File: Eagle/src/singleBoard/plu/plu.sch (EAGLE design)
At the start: 10 parts, among them J1 5787834-2

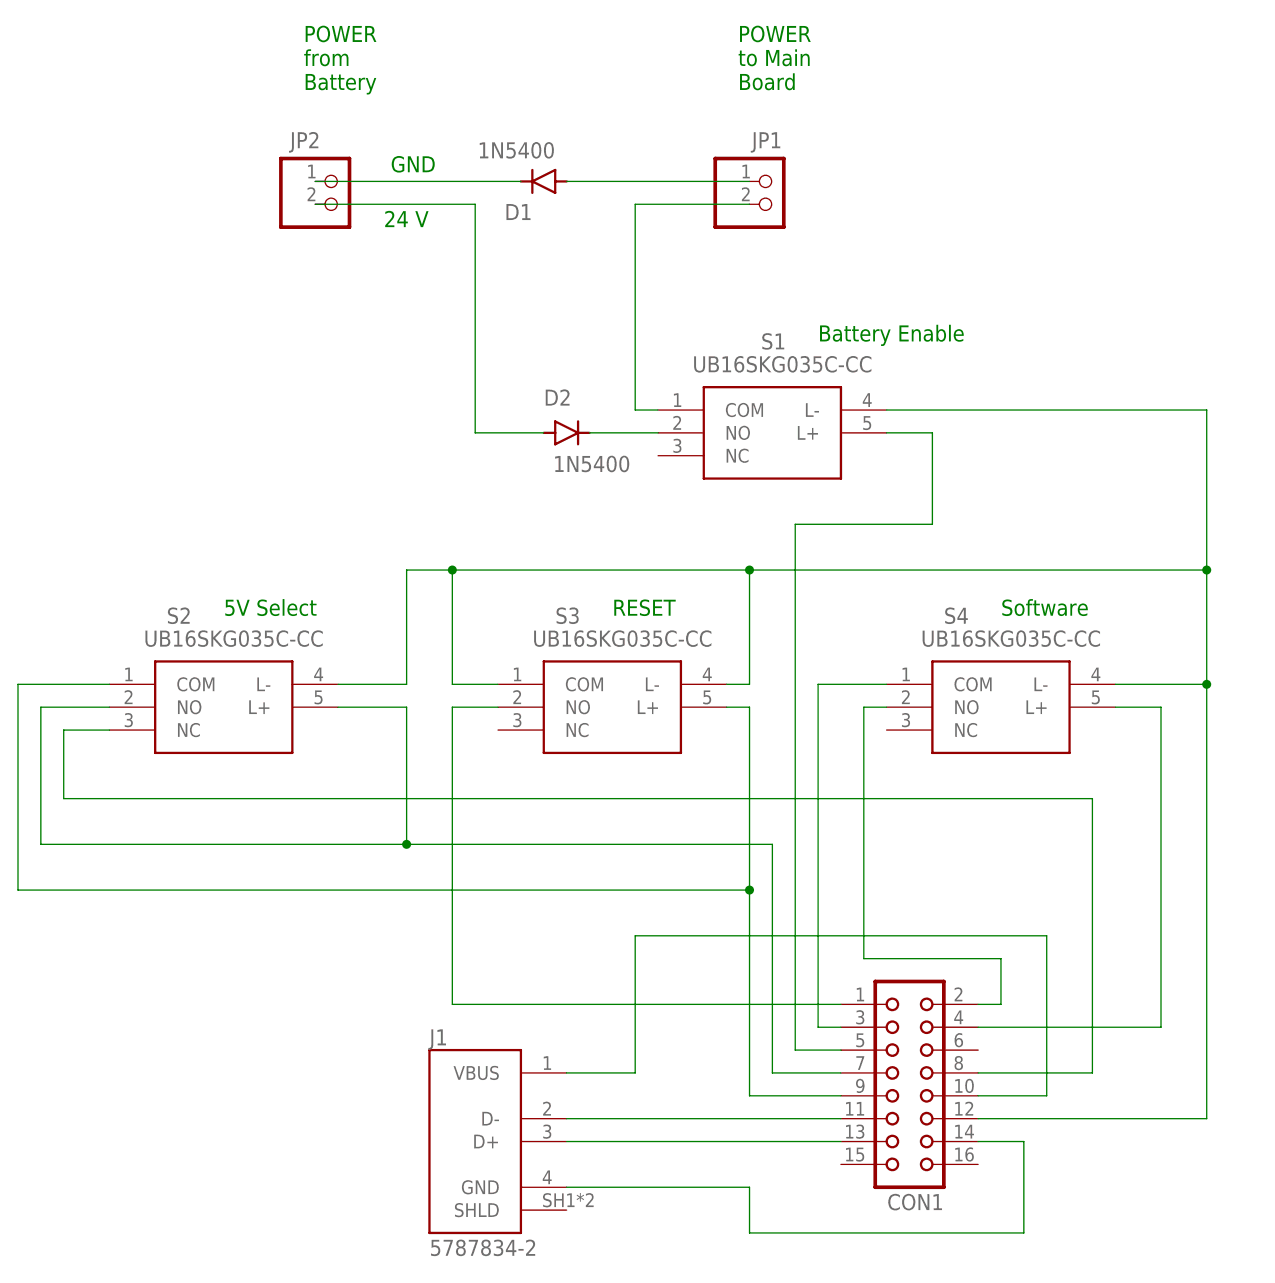
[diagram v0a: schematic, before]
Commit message: fix plu spacing issues found in flatcam
version P2 of PLU has a bunch of fixes to fix places where there were passages between traces, or between traces and pads that were too narrow for a 1/32 inch mill bit to pass through. 2 weren't fixable, and I added jumpers to dodge the issue. The rest of the 7 issues were resolved by small adjustments to trace locations
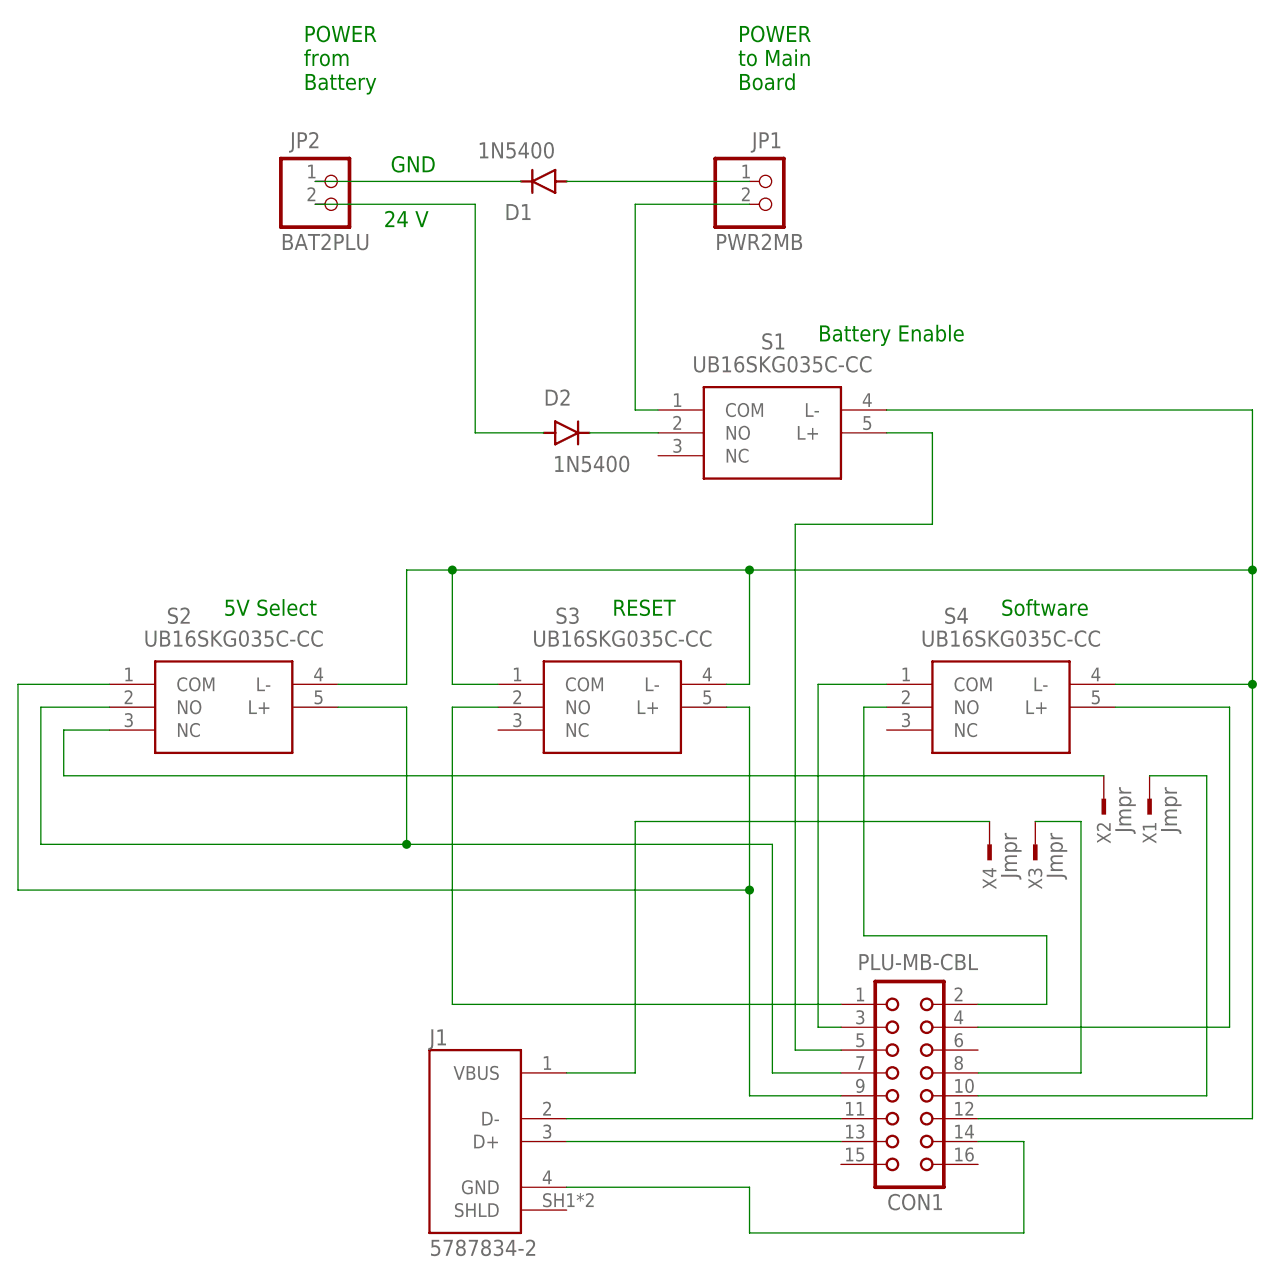
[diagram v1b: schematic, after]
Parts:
- added X1, X2, X3, X4: Jmpr, con-samtec:TSW-101-07-G-S
- CON1: value (none) -> PLU-MB-CBL
- JP1: value (none) -> PWR2MB
- JP2: value (none) -> BAT2PLU
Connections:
- new net N$25: S2.NC, X2.1
- new net N$28: CON1.8, X3.1
- net N$18: now also CON1.10, X1.1; no longer CON1.8, S2.NC
- net N$8: now also X4.1; no longer CON1.10
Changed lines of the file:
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@@
 </classes>
 <parts>
-<part name="CON1" library="con-harting" library_urn="urn:adsk.eagle:library:151" deviceset="CON16" device="" package3d_urn="urn:adsk.eagle:package:7118/1"/>
-<part name="JP2" library="pinhead" library_urn="urn:adsk.eagle:library:325" deviceset="PINHD-1X2" device="" package3d_urn="urn:adsk.eagle:package:22435/2"/>
+<part name="CON1" library="con-harting" library_urn="urn:adsk.eagle:library:151" deviceset="CON16" device="" package3d_urn="urn:adsk.eagle:package:7118/1" value="PLU-MB-CBL"/>
+<part name="JP2" library="pinhead" library_urn="urn:adsk.eagle:library:325" deviceset="PINHD-1X2" device="" package3d_urn="urn:adsk.eagle:package:22435/2" value="BAT2PLU"/>
 <part name="S1" library="UB16SKG035C-CC" deviceset="UB16SKG035C-CC" device=""/>
 <part name="S2" library="UB16SKG035C-CC" deviceset="UB16SKG035C-CC" device=""/>
 <part name="S3" library="UB16SKG035C-CC" deviceset="UB16SKG035C-CC" device=""/>
 <part name="S4" library="UB16SKG035C-CC" deviceset="UB16SKG035C-CC" device=""/>
-<part name="JP1" library="pinhead" library_urn="urn:adsk.eagle:library:325" deviceset="PINHD-1X2" device="" package3d_urn="urn:adsk.eagle:package:22435/2"/>
+<part name="JP1" library="pinhead" library_urn="urn:adsk.eagle:library:325" deviceset="PINHD-1X2" device="" package3d_urn="urn:adsk.eagle:package:22435/2" value="PWR2MB"/>
 <part name="J1" library="5787834-2" deviceset="5787834-2" device=""/>
 <part name="D1" library="diode" library_urn="urn:adsk.eagle:library:210" deviceset="1N5400" device="" package3d_urn="urn:adsk.eagle:package:43365/1"/>
 <part name="D2" library="diode" library_urn="urn:adsk.eagle:library:210" deviceset="1N5400" device="" package3d_urn="urn:adsk.eagle:package:43365/1"/>
+<part name="X1" library="con-samtec" library_urn="urn:adsk.eagle:library:184" deviceset="TSW-101-*-G-S" device="" technology="07" value="Jmpr"/>
+<part name="X2" library="con-samtec" library_urn="urn:adsk.eagle:library:184" deviceset="TSW-101-*-G-S" device="" technology="07" value="Jmpr"/>
+<part name="X3" library="con-samtec" library_urn="urn:adsk.eagle:library:184" deviceset="TSW-101-*-G-S" device="" technology="07" value="Jmpr"/>
+<part name="X4" library="con-samtec" library_urn="urn:adsk.eagle:library:184" deviceset="TSW-101-*-G-S" device="" technology="07" value="Jmpr"/>
 </parts>
 <sheets>
@@
 <instances>
 <instance part="CON1" gate="G$1" x="71.12" y="-116.84" smashed="yes" rot="R180">
-<attribute name="VALUE" x="74.93" y="-101.6" size="1.778" layer="96" rot="R180"/>
+<attribute name="VALUE" x="78.74" y="-101.092" size="1.778" layer="96" rot="R180"/>
 <attribute name="NAME" x="74.93" y="-127.762" size="1.778" layer="95" rot="R180"/>
 </instance>
@@
 <attribute name="NAME" x="30.48" y="-40.1574" size="1.778" layer="95"/>
 <attribute name="VALUE" x="31.496" y="-47.5234" size="1.778" layer="96"/>
+</instance>
+<instance part="X1" gate="-1" x="97.79" y="-83.82" smashed="yes" rot="R270">
+<attribute name="VALUE" x="99.06" y="-82.55" size="1.778" layer="96" rot="R270"/>
+<attribute name="NAME" x="97.028" y="-86.36" size="1.524" layer="95" rot="R270"/>
+</instance>
+<instance part="X2" gate="-1" x="92.71" y="-83.82" smashed="yes" rot="R270">
+<attribute name="VALUE" x="93.98" y="-82.55" size="1.778" layer="96" rot="R270"/>
+<attribute name="NAME" x="91.948" y="-86.36" size="1.524" layer="95" rot="R270"/>
+</instance>
+<instance part="X3" gate="-1" x="85.09" y="-88.9" smashed="yes" rot="R270">
+<attribute name="VALUE" x="86.36" y="-87.63" size="1.778" layer="96" rot="R270"/>
+<attribute name="NAME" x="84.328" y="-91.44" size="1.524" layer="95" rot="R270"/>
+</instance>
+<instance part="X4" gate="-1" x="80.01" y="-88.9" smashed="yes" rot="R270">
+<attribute name="VALUE" x="81.28" y="-87.63" size="1.778" layer="96" rot="R270"/>
+<attribute name="NAME" x="79.248" y="-91.44" size="1.524" layer="95" rot="R270"/>
 </instance>
 </instances>
@@
 <pinref part="JP1" gate="G$1" pin="2"/>
 <wire x1="40.64" y1="-17.78" x2="53.34" y2="-17.78" width="1.27" layer="91"/>
-</segment>
-</net>
-<net name="N$8" class="0">
-<segment>
-<wire x1="33.02" y1="-114.3" x2="40.64" y2="-114.3" width="0.1524" layer="91"/>
-<pinref part="J1" gate="G$1" pin="VBUS"/>
-<wire x1="40.64" y1="-114.3" x2="40.64" y2="-99.06" width="0.1524" layer="91"/>
-<wire x1="40.64" y1="-99.06" x2="86.36" y2="-99.06" width="0.1524" layer="91"/>
-<wire x1="86.36" y1="-99.06" x2="86.36" y2="-116.84" width="0.1524" layer="91"/>
-<pinref part="CON1" gate="G$1" pin="10"/>
-<wire x1="78.74" y1="-116.84" x2="86.36" y2="-116.84" width="0.1524" layer="91"/>
 </segment>
 </net>
@@
 <wire x1="66.04" y1="-73.66" x2="68.58" y2="-73.66" width="0.1524" layer="91"/>
 <pinref part="CON1" gate="G$1" pin="2"/>
-<wire x1="78.74" y1="-106.68" x2="81.28" y2="-106.68" width="0.1524" layer="91"/>
-<wire x1="81.28" y1="-106.68" x2="81.28" y2="-101.6" width="0.1524" layer="91"/>
-<wire x1="81.28" y1="-101.6" x2="66.04" y2="-101.6" width="0.1524" layer="91"/>
-<wire x1="66.04" y1="-101.6" x2="66.04" y2="-73.66" width="0.1524" layer="91"/>
+<wire x1="66.04" y1="-99.06" x2="66.04" y2="-73.66" width="0.1524" layer="91"/>
+<wire x1="66.04" y1="-99.06" x2="86.36" y2="-99.06" width="0.1524" layer="91"/>
+<wire x1="86.36" y1="-99.06" x2="86.36" y2="-106.68" width="0.1524" layer="91"/>
+<wire x1="86.36" y1="-106.68" x2="78.74" y2="-106.68" width="0.1524" layer="91"/>
 </segment>
 </net>
@@
 <segment>
 <pinref part="CON1" gate="G$1" pin="4"/>
-<wire x1="78.74" y1="-109.22" x2="99.06" y2="-109.22" width="0.1524" layer="91"/>
-<wire x1="99.06" y1="-109.22" x2="99.06" y2="-73.66" width="0.1524" layer="91"/>
+<wire x1="78.74" y1="-109.22" x2="106.68" y2="-109.22" width="0.1524" layer="91"/>
+<wire x1="106.68" y1="-109.22" x2="106.68" y2="-73.66" width="0.1524" layer="91"/>
 <pinref part="S4" gate="G$1" pin="L+"/>
-<wire x1="99.06" y1="-73.66" x2="93.98" y2="-73.66" width="0.1524" layer="91"/>
+<wire x1="106.68" y1="-73.66" x2="93.98" y2="-73.66" width="0.1524" layer="91"/>
 </segment>
 </net>
@@
 </segment>
 </net>
-<net name="N$18" class="0">
-<segment>
-<wire x1="91.44" y1="-114.3" x2="91.44" y2="-83.82" width="0.1524" layer="91"/>
-<wire x1="91.44" y1="-83.82" x2="-22.86" y2="-83.82" width="0.1524" layer="91"/>
-<wire x1="-22.86" y1="-83.82" x2="-22.86" y2="-76.2" width="0.1524" layer="91"/>
-<pinref part="S2" gate="G$1" pin="NC"/>
-<wire x1="-22.86" y1="-76.2" x2="-17.78" y2="-76.2" width="0.1524" layer="91"/>
-<pinref part="CON1" gate="G$1" pin="8"/>
-<wire x1="78.74" y1="-114.3" x2="91.44" y2="-114.3" width="0.1524" layer="91"/>
-</segment>
-</net>
 <net name="N$19" class="0">
 <segment>
@@
 <segment>
 <pinref part="CON1" gate="G$1" pin="12"/>
-<wire x1="78.74" y1="-119.38" x2="104.14" y2="-119.38" width="0.1524" layer="91"/>
-<wire x1="104.14" y1="-119.38" x2="104.14" y2="-71.12" width="0.1524" layer="91"/>
+<wire x1="78.74" y1="-119.38" x2="109.22" y2="-119.38" width="0.1524" layer="91"/>
+<wire x1="109.22" y1="-119.38" x2="109.22" y2="-71.12" width="0.1524" layer="91"/>
 <pinref part="S1" gate="G$1" pin="L-"/>
-<wire x1="104.14" y1="-71.12" x2="104.14" y2="-58.42" width="0.1524" layer="91"/>
-<wire x1="104.14" y1="-58.42" x2="104.14" y2="-40.64" width="0.1524" layer="91"/>
-<wire x1="104.14" y1="-40.64" x2="68.58" y2="-40.64" width="0.1524" layer="91"/>
-<wire x1="104.14" y1="-58.42" x2="53.34" y2="-58.42" width="0.1524" layer="91"/>
-<junction x="104.14" y="-58.42"/>
+<wire x1="109.22" y1="-71.12" x2="109.22" y2="-58.42" width="0.1524" layer="91"/>
+<wire x1="109.22" y1="-58.42" x2="109.22" y2="-40.64" width="0.1524" layer="91"/>
+<wire x1="109.22" y1="-40.64" x2="68.58" y2="-40.64" width="0.1524" layer="91"/>
+<wire x1="109.22" y1="-58.42" x2="53.34" y2="-58.42" width="0.1524" layer="91"/>
+<junction x="109.22" y="-58.42"/>
 <wire x1="53.34" y1="-58.42" x2="20.32" y2="-58.42" width="0.1524" layer="91"/>
 <wire x1="20.32" y1="-58.42" x2="15.24" y2="-58.42" width="0.1524" layer="91"/>
@@
 <junction x="53.34" y="-58.42"/>
 <pinref part="S4" gate="G$1" pin="L-"/>
-<wire x1="93.98" y1="-71.12" x2="104.14" y2="-71.12" width="0.1524" layer="91"/>
-<junction x="104.14" y="-71.12"/>
+<wire x1="93.98" y1="-71.12" x2="109.22" y2="-71.12" width="0.1524" layer="91"/>
+<junction x="109.22" y="-71.12"/>
 <pinref part="S3" gate="G$1" pin="COM"/>
 <wire x1="25.4" y1="-71.12" x2="20.32" y2="-71.12" width="0.1524" layer="91"/>
@@
 </segment>
 </net>
+<net name="N$18" class="0">
+<segment>
+<pinref part="CON1" gate="G$1" pin="10"/>
+<wire x1="78.74" y1="-116.84" x2="104.14" y2="-116.84" width="0.1524" layer="91"/>
+<wire x1="104.14" y1="-116.84" x2="104.14" y2="-81.28" width="0.1524" layer="91"/>
+<pinref part="X1" gate="-1" pin="1"/>
+<wire x1="97.79" y1="-81.28" x2="104.14" y2="-81.28" width="0.1524" layer="91"/>
+</segment>
+</net>
+<net name="N$25" class="0">
+<segment>
+<pinref part="S2" gate="G$1" pin="NC"/>
+<wire x1="-22.86" y1="-81.28" x2="-22.86" y2="-76.2" width="0.1524" layer="91"/>
+<wire x1="-22.86" y1="-76.2" x2="-17.78" y2="-76.2" width="0.1524" layer="91"/>
+<pinref part="X2" gate="-1" pin="1"/>
+<wire x1="-22.86" y1="-81.28" x2="92.71" y2="-81.28" width="0.1524" layer="91"/>
+</segment>
+</net>
+<net name="N$8" class="0">
+<segment>
+<pinref part="J1" gate="G$1" pin="VBUS"/>
+<wire x1="33.02" y1="-114.3" x2="40.64" y2="-114.3" width="0.1524" layer="91"/>
+<pinref part="X4" gate="-1" pin="1"/>
+<wire x1="80.01" y1="-86.36" x2="40.64" y2="-86.36" width="0.1524" layer="91"/>
+<wire x1="40.64" y1="-86.36" x2="40.64" y2="-114.3" width="0.1524" layer="91"/>
+</segment>
+</net>
+<net name="N$28" class="0">
+<segment>
+<pinref part="X3" gate="-1" pin="1"/>
+<wire x1="85.09" y1="-86.36" x2="90.17" y2="-86.36" width="0.1524" layer="91"/>
+<wire x1="90.17" y1="-86.36" x2="90.17" y2="-114.3" width="0.1524" layer="91"/>
+<pinref part="CON1" gate="G$1" pin="8"/>
+<wire x1="90.17" y1="-114.3" x2="78.74" y2="-114.3" width="0.1524" layer="91"/>
+</segment>
+</net>
